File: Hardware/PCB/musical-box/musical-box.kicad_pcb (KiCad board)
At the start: 4 copper layers, 70 x 60 mm, 190 parts, among them J1 power, J201 PSU, J202 Jack-DC, J203 BATT, J401 SPI Display, J402 Rotary Encoder 1, J403 I2C Display, J404 Rotary Encoder 2, J405 WS2812, J501 spk_out, J502 aux in, J503 line in, P201 USB_C, P202 ICT-Point, P203 ICT-Point, P204 ICT-Point, Q201 IRFHM9331, Q204 IRF9362, Q301 BC846BDW1, SW301 boot, SW302 reset, U201 STUSB4500QTR, U202 MP2615, U203 TPS56339, U204 TLV75733PDBV, U205 TLV75733PDBV, U206 TLV803EC30DBZR, U207 TPD2EUSB30A, U301 CH340C, U302 ESP32-WROVER, U401 PCF8574ATS, U501 SPH0644HM4H-1, U502 SPH0644HM4H-1, U503 TAS5754MDCA

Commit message: Reduce number of unique parts
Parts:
- C204, C208, C209, C214, C215, C503, C507, C517, C518, C521, C524: value 1u -> 2.2u
- C221, C226, C301, C303, C402, C406: value 10u -> 22u
- C508, C513, C515, C520: value 220n -> 100n
- L203: value XAL6030-562 -> 6.8u
- R106, R107: value 4,7k -> 1k
- R206: value 100R -> 220R
- R208: value 22k -> 10k
- R223: value 30R -> 10R
- R409: value 46,4k -> 10k
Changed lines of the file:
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@@
       (effects (font (size 1 1) (thickness 0.15)) (justify mirror))
     )
-    (fp_text value 46,4k (at 0 -1.43 90) (layer B.Fab)
+    (fp_text value 10k (at 0 -1.43 90) (layer B.Fab)
       (effects (font (size 1 1) (thickness 0.15)) (justify mirror))
     )
@@
       (effects (font (size 1 1) (thickness 0.15)) (justify mirror))
     )
-    (fp_text value 30R (at 0 -1.43) (layer B.Fab)
+    (fp_text value 10R (at 0 -1.43) (layer B.Fab)
       (effects (font (size 1 1) (thickness 0.15)) (justify mirror))
     )
@@
       (effects (font (size 1 1) (thickness 0.15)) (justify mirror))
     )
-    (fp_text value 10u (at 0 -1.43) (layer B.Fab) hide
+    (fp_text value 22u (at 0 -1.43) (layer B.Fab) hide
       (effects (font (size 1 1) (thickness 0.15)) (justify mirror))
     )
@@
       (effects (font (size 1 1) (thickness 0.15)) (justify mirror))
     )
-    (fp_text value 4,7k (at 0 -1.43 270) (layer B.Fab) hide
+    (fp_text value 1k (at 0 -1.43 270) (layer B.Fab) hide
       (effects (font (size 1 1) (thickness 0.15)) (justify mirror))
     )
@@
       (effects (font (size 1 1) (thickness 0.15)) (justify mirror))
     )
-    (fp_text value 4,7k (at 0 -1.43 270) (layer B.Fab) hide
+    (fp_text value 1k (at 0 -1.43 270) (layer B.Fab) hide
       (effects (font (size 1 1) (thickness 0.15)) (justify mirror))
     )
@@
       (effects (font (size 1 1) (thickness 0.15)) (justify mirror))
     )
-    (fp_text value 22k (at 0 -1.43 90) (layer B.Fab) hide
+    (fp_text value 10k (at 0 -1.43 90) (layer B.Fab) hide
       (effects (font (size 1 1) (thickness 0.15)) (justify mirror))
     )
@@
       (effects (font (size 1 1) (thickness 0.15)) (justify mirror))
     )
-    (fp_text value 100R (at 0 -1.43 90) (layer B.Fab) hide
+    (fp_text value 220R (at 0 -1.43 90) (layer B.Fab) hide
       (effects (font (size 1 1) (thickness 0.15)) (justify mirror))
     )
@@
       (effects (font (size 1 1) (thickness 0.15)))
     )
-    (fp_text value XAL6030-562 (at 0 -4 90) (layer F.Fab) hide
+    (fp_text value 6.8u (at 0 -4 90) (layer F.Fab) hide
       (effects (font (size 1 1) (thickness 0.15)))
     )
@@
       (effects (font (size 1 1) (thickness 0.15)))
     )
-    (fp_text value 1u (at 0 1.43 90) (layer F.Fab) hide
+    (fp_text value 2.2u (at 0 1.43 90) (layer F.Fab) hide
       (effects (font (size 1 1) (thickness 0.15)))
     )
@@
       (effects (font (size 1 1) (thickness 0.15)))
     )
-    (fp_text value 1u (at 0 1.43 90) (layer F.Fab) hide
+    (fp_text value 2.2u (at 0 1.43 90) (layer F.Fab) hide
       (effects (font (size 1 1) (thickness 0.15)))
     )
@@
       (effects (font (size 1 1) (thickness 0.15)) (justify mirror))
     )
-    (fp_text value 220n (at 0 -1.43 270) (layer B.Fab) hide
+    (fp_text value 100n (at 0 -1.43 270) (layer B.Fab) hide
       (effects (font (size 1 1) (thickness 0.15)) (justify mirror))
     )
@@
       (effects (font (size 1 1) (thickness 0.15)))
     )
-    (fp_text value 1u (at 0 1.43 90) (layer F.Fab) hide
+    (fp_text value 2.2u (at 0 1.43 90) (layer F.Fab) hide
       (effects (font (size 1 1) (thickness 0.15)))
     )
@@
       (effects (font (size 1 1) (thickness 0.15)))
     )
-    (fp_text value 1u (at 0 1.43 90) (layer F.Fab) hide
+    (fp_text value 2.2u (at 0 1.43 90) (layer F.Fab) hide
       (effects (font (size 1 1) (thickness 0.15)))
     )
@@
       (effects (font (size 1 1) (thickness 0.15)))
     )
-    (fp_text value 220n (at 0 1.43 90) (layer F.Fab) hide
+    (fp_text value 100n (at 0 1.43 90) (layer F.Fab) hide
       (effects (font (size 1 1) (thickness 0.15)))
     )
@@
       (effects (font (size 1 1) (thickness 0.15)))
     )
-    (fp_text value 220n (at 0 1.43 90) (layer F.Fab) hide
+    (fp_text value 100n (at 0 1.43 90) (layer F.Fab) hide
       (effects (font (size 1 1) (thickness 0.15)))
     )
@@
       (effects (font (size 1 1) (thickness 0.15)) (justify mirror))
     )
-    (fp_text value 220n (at 0 -1.43 270) (layer B.Fab) hide
+    (fp_text value 100n (at 0 -1.43 270) (layer B.Fab) hide
       (effects (font (size 1 1) (thickness 0.15)) (justify mirror))
     )
@@
       (effects (font (size 1 1) (thickness 0.15)))
     )
-    (fp_text value 1u (at 0 1.43 90) (layer F.Fab) hide
+    (fp_text value 2.2u (at 0 1.43 90) (layer F.Fab) hide
       (effects (font (size 1 1) (thickness 0.15)))
     )
@@
       (effects (font (size 1 1) (thickness 0.15)))
     )
-    (fp_text value 1u (at 0 1.43 90) (layer F.Fab) hide
+    (fp_text value 2.2u (at 0 1.43 90) (layer F.Fab) hide
       (effects (font (size 1 1) (thickness 0.15)))
     )
@@
       (effects (font (size 1 1) (thickness 0.15)) (justify mirror))
     )
-    (fp_text value 10u (at 0 -1.43 90) (layer B.Fab) hide
+    (fp_text value 22u (at 0 -1.43 90) (layer B.Fab) hide
       (effects (font (size 1 1) (thickness 0.15)) (justify mirror))
     )
@@
       (effects (font (size 1 1) (thickness 0.15)) (justify mirror))
     )
-    (fp_text value 10u (at 0 -1.43) (layer B.Fab) hide
+    (fp_text value 22u (at 0 -1.43) (layer B.Fab) hide
       (effects (font (size 1 1) (thickness 0.15)) (justify mirror))
     )
@@
       (effects (font (size 1 1) (thickness 0.15)))
     )
-    (fp_text value 10u (at 0 1.43 90) (layer F.Fab) hide
+    (fp_text value 22u (at 0 1.43 90) (layer F.Fab) hide
       (effects (font (size 1 1) (thickness 0.15)))
     )
@@
       (effects (font (size 1 1) (thickness 0.15)) (justify mirror))
     )
-    (fp_text value 10u (at 0 -1.43 270) (layer B.Fab) hide
+    (fp_text value 22u (at 0 -1.43 270) (layer B.Fab) hide
       (effects (font (size 1 1) (thickness 0.15)) (justify mirror))
     )
@@
       (effects (font (size 1 1) (thickness 0.15)) (justify mirror))
     )
-    (fp_text value 10u (at 0 -1.43 270) (layer B.Fab) hide
+    (fp_text value 22u (at 0 -1.43 270) (layer B.Fab) hide
       (effects (font (size 1 1) (thickness 0.15)) (justify mirror))
     )
@@
       (effects (font (size 1 1) (thickness 0.15)) (justify mirror))
     )
-    (fp_text value 1u (at 0 -1.43 90) (layer B.Fab) hide
+    (fp_text value 2.2u (at 0 -1.43 90) (layer B.Fab) hide
       (effects (font (size 1 1) (thickness 0.15)) (justify mirror))
     )
@@
       (effects (font (size 1 1) (thickness 0.15)) (justify mirror))
     )
-    (fp_text value 1u (at 0 -1.43 90) (layer B.Fab) hide
+    (fp_text value 2.2u (at 0 -1.43 90) (layer B.Fab) hide
       (effects (font (size 1 1) (thickness 0.15)) (justify mirror))
     )
@@
       (effects (font (size 1 1) (thickness 0.15)) (justify mirror))
     )
-    (fp_text value 1u (at 0 -1.43) (layer B.Fab) hide
+    (fp_text value 2.2u (at 0 -1.43) (layer B.Fab) hide
       (effects (font (size 1 1) (thickness 0.15)) (justify mirror))
     )
@@
       (effects (font (size 1 1) (thickness 0.15)) (justify mirror))
     )
-    (fp_text value 1u (at 0 -1.43) (layer B.Fab) hide
+    (fp_text value 2.2u (at 0 -1.43) (layer B.Fab) hide
       (effects (font (size 1 1) (thickness 0.15)) (justify mirror))
     )
@@
       (effects (font (size 1 1) (thickness 0.15)) (justify mirror))
     )
-    (fp_text value 1u (at 0 -1.43 270) (layer B.Fab) hide
+    (fp_text value 2.2u (at 0 -1.43 270) (layer B.Fab) hide
       (effects (font (size 1 1) (thickness 0.15)) (justify mirror))
     )

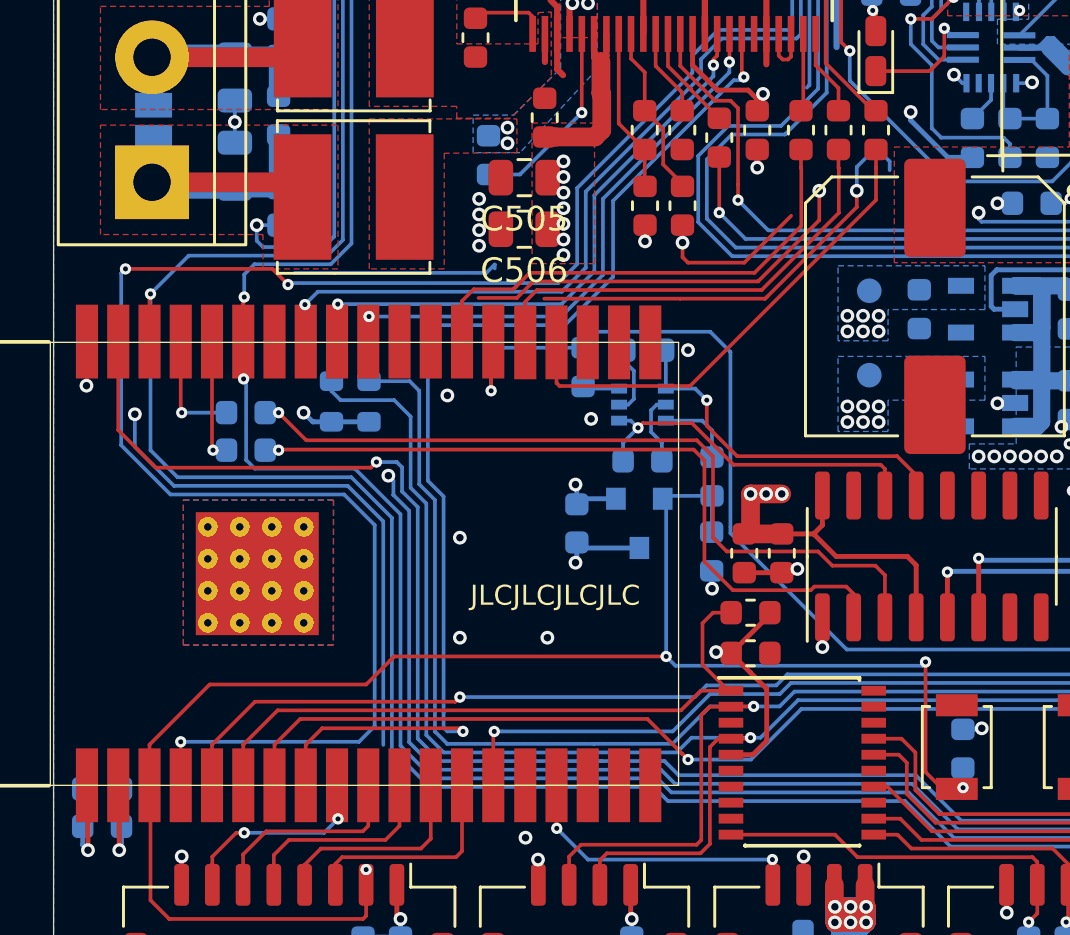
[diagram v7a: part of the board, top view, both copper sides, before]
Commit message: Add JTAG connector and move to SOT-23 single transistors
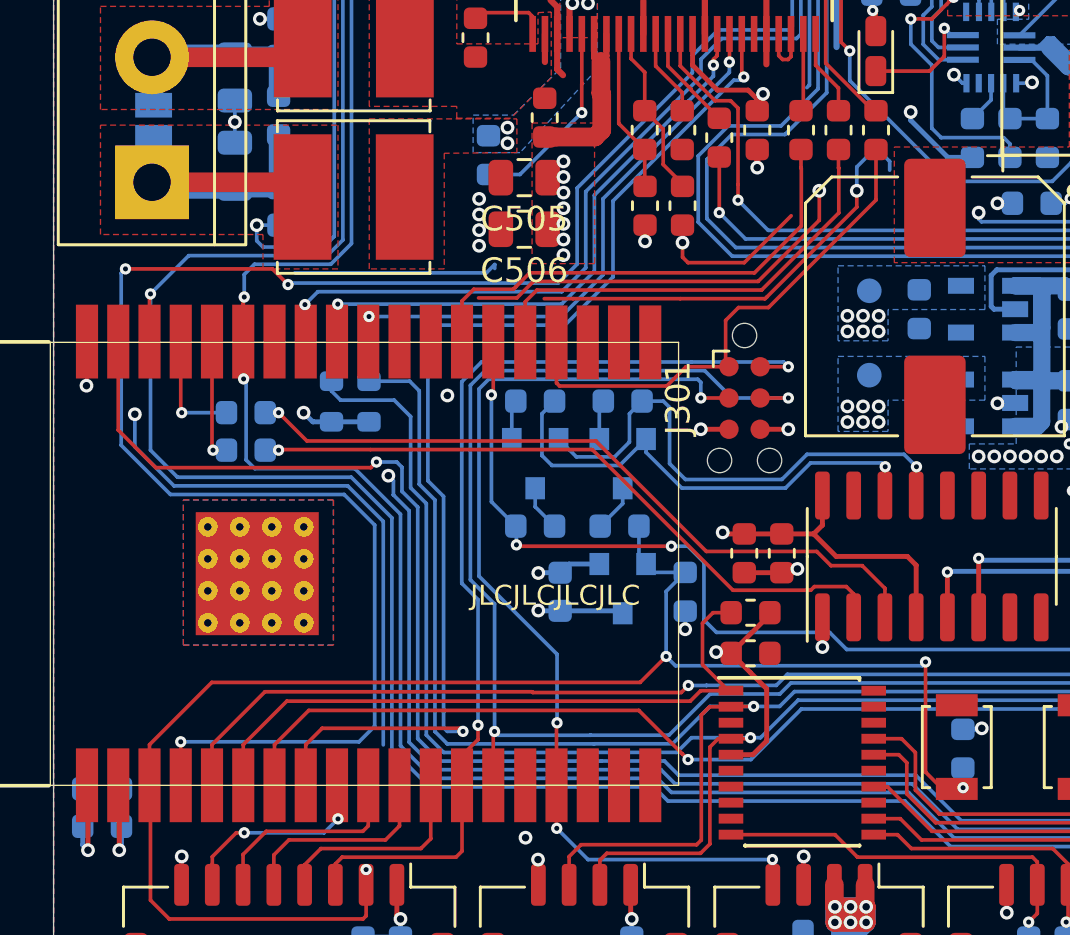
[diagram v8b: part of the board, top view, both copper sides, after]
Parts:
- added J301: JTAG, Connector:Tag-Connect_TC2030-IDC-NL_2x03_P1.27mm_Vertical, F.Cu at (378.1, 159.8)
- added Q302: BC848, Package_TO_SOT_SMD:SOT-23, B.Cu at (369.6, 162.4)
- C301, C303, C402, C406: value 22u -> 2.2u
- J503: value line in -> line out
- Q301: value BC846BDW1 -> BC848; footprint Package_TO_SOT_SMD:SOT-363_SC-70-6 -> Package_TO_SOT_SMD:SOT-23
- moved R309 6.75 mm to (369.6, 165.0), turned to 0 degrees
- moved R308 4.99 mm to (369.6, 159.9), turned to 0 degrees
- moved R304 4.26 mm to (373.0, 165.0), turned to 0 degrees
- moved C227 2.86 mm to (370.6, 167.6)
- moved U206 2.74 mm to (373.1, 167.5)
- moved Q301 2.53 mm to (373.1, 162.4), turned to 270 degrees
- moved R305 2.25 mm to (373.1, 159.9)
- moved R222 1.96 mm to (375.7, 167.6)
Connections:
- P201 pad A8: Net-(P201-PadA8) -> (no net)
- P201 pad B8: Net-(P201-PadB8) -> (no net)
- Q301 pad 1: /Microcontroller/DTR -> Net-(Q301-Pad1)
- Q301 pad 2: Net-(Q301-Pad2) -> /Microcontroller/RTS
- R305 pad 1: Net-(Q301-Pad5) -> Net-(Q301-Pad1)
- R308 pad 1: Net-(Q301-Pad2) -> Net-(Q302-Pad1)
- R309 pad 2: Net-(Q301-Pad6) -> Net-(Q302-Pad3)
- U201 pad 14: Net-(U201-Pad14) -> (no net)
- U201 pad 15: Net-(U201-Pad15) -> (no net)
- U201 pad 17: Net-(U201-Pad17) -> (no net)
- U201 pad 20: Net-(U201-Pad20) -> (no net)
- U201 pad 3: Net-(U201-Pad3) -> (no net)
- U202 pad 12: Net-(U202-Pad12) -> (no net)
- U203 pad 5: Net-(U203-Pad5) -> (no net)
- U301 pad 10: Net-(U301-Pad10) -> (no net)
- U301 pad 11: Net-(U301-Pad11) -> (no net)
- U301 pad 12: Net-(U301-Pad12) -> (no net)
- U301 pad 15: Net-(U301-Pad15) -> (no net)
- U301 pad 7: Net-(U301-Pad7) -> (no net)
- U301 pad 8: Net-(U301-Pad8) -> (no net)
- U301 pad 9: Net-(U301-Pad9) -> (no net)
- U302 pad 17: Net-(U302-Pad17) -> (no net)
- U302 pad 18: Net-(U302-Pad18) -> (no net)
- U302 pad 19: Net-(U302-Pad19) -> (no net)
- U302 pad 20: Net-(U302-Pad20) -> (no net)
- U302 pad 21: Net-(U302-Pad21) -> (no net)
- U302 pad 22: Net-(U302-Pad22) -> (no net)
- U401 pad 13: Net-(U401-Pad13) -> (no net)
- U401 pad 18: Net-(U401-Pad18) -> (no net)
- U401 pad 19: Net-(U401-Pad19) -> (no net)
- U401 pad 20: Net-(U401-Pad20) -> (no net)
- U401 pad 3: Net-(U401-Pad3) -> (no net)
- U401 pad 8: Net-(U401-Pad8) -> (no net)
- U503 pad 19: /Audio Output/GPIO1 -> (no net)
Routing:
- net /Microcontroller/IO14: track 8.89 -> 40.7 mm, vias 0 -> 2
- net /Microcontroller/IO12: track 68.7 -> 98.1 mm, vias 4 -> 5
- net /Microcontroller/IO13: track 12.1 -> 40.5 mm, vias 2 -> 4
- net +3V3: track 184.8 -> 159.3 mm, vias 28 -> 27
- net /Microcontroller/DTR: track 14.7 -> 20.9 mm
- net /Microcontroller/RTS: track 14.4 -> 19.8 mm
- net /Microcontroller/IO00: track 50.7 -> 47.7 mm, vias 3 -> 5
- net Net-(Q301-Pad2): track 2.93 -> 0.00 mm
- net /Microcontroller/~RESET: track 67.9 -> 65.1 mm
- net Net-(Q301-Pad5): track 2.83 -> 0.00 mm
- net Net-(R302-Pad2): track 29.8 -> 27.4 mm
- net Net-(R303-Pad2): track 31.6 -> 29.3 mm
- net Net-(Q302-Pad3): track 0.00 -> 1.87 mm
- net Net-(Q302-Pad1): track 0.00 -> 1.61 mm
- net Net-(Q301-Pad1): track 0.00 -> 1.61 mm
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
